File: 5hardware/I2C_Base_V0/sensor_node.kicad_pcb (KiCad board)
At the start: 2 copper layers, 99.5 x 99.5 mm, 264 parts, among them J2 PJ-320D-A, J3 Conn_02x06_Top_Bottom, J4 Conn_01x19_Socket, J5 Conn_01x19_Socket, J6 Conn_01x06_Socket, J7 Conn_01x04_Pin, J8 Conn_01x04_Pin, P1 S3B-PH-SM4-TB, P2 S4B-PH-SM4-TB, P3 S3B-PH-SM4-TB, Q2 Si2371EDS, Q3 Si2371EDS, SW2 SW_Push, SW3 SW_Push, U10 ESP-12F, U12 APDS-9960, U14 DS3231M, U3 CR2450, U4 CH32V003F4P6, U5 SHT31-DIS, U6 DS1307Z+, U7 XC6206PxxxMR, U8 TPL5110, U9 BH1750FVI-TR, Y1 Crystal, Y2 Crystal

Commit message: update PCB.
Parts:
- removed the C1 at (146.2, 141.2)
- removed the C1 at (96.2, 141.2)
- removed the C1 at (96.2, 91.2)
- removed the C1 at (146.2, 91.2)
- removed the C2 at (107.9, 75.8)
- removed the C2 at (57.9, 75.8)
- removed the C2 at (57.9, 125.8)
- removed the C2 at (107.9, 125.8)
- removed the C3 at (108.0, 64.8)
- removed the C3 at (58.0, 64.8)
- removed the C3 at (58.0, 114.8)
- removed the C3 at (108.0, 114.8)
- removed the C5 at (143.8, 125.5)
- removed the C5 at (93.8, 75.5)
- removed the C5 at (93.8, 125.5)
- removed the C5 at (143.8, 75.5)
- removed the C6 at (143.8, 70.8)
- removed the C6 at (93.8, 120.8)
- removed the C6 at (93.8, 70.8)
- removed the C6 at (143.8, 120.8)
- removed the D1 at (127.6, 77.2)
- removed the D1 at (127.6, 127.2)
- removed the D1 at (77.6, 77.2)
- removed the D1 at (77.6, 127.2)
- removed D10 (x4): LED, LED_SMD:LED_0603_1608Metric
- removed the D2 at (88.1, 113.8)
- removed the D2 at (138.1, 63.8)
- removed the D2 at (88.1, 63.8)
- removed the D2 at (138.1, 113.8)
- removed the D3 at (130.5, 124.0)
- removed the D3 at (80.5, 124.0)
- removed the D3 at (80.5, 74.0)
- removed the D3 at (130.5, 74.0)
- removed the D4 at (140.0, 120.5)
- removed the D4 at (90.0, 120.5)
- removed the D4 at (90.0, 70.5)
- removed the D4 at (140.0, 70.5)
- removed the D5 at (81.5, 90.5)
- removed the D5 at (131.5, 90.5)
- removed the D5 at (131.5, 140.5)
- removed the D5 at (81.5, 140.5)
- removed the D6 at (76.0, 108.8)
- removed the D6 at (126.0, 108.8)
- removed the D6 at (126.0, 58.8)
- removed the D6 at (76.0, 58.8)
- removed the J2 at (75.4, 87.7)
- removed the J2 at (125.4, 137.7)
- removed the J2 at (75.4, 137.7)
- removed the J2 at (125.4, 87.7)
- removed the J3 at (94.9, 53.6)
- removed the J3 at (144.9, 53.6)
- removed the J3 at (94.9, 103.6)
- removed the J3 at (144.9, 103.6)
- removed the J4 at (97.7, 99.8)
- removed the J4 at (97.7, 49.8)
- removed the J4 at (147.7, 99.8)
- removed the J4 at (147.7, 49.8)
- removed the J5 at (97.7, 46.0)
- removed the J5 at (147.7, 46.0)
- removed the J5 at (147.7, 96.0)
- removed the J5 at (97.7, 96.0)
- removed J6 (x4): Conn_01x06_Socket, Connector_PinHeader_2.00mm:PinHeader_1x06_P2.00mm_Vertical
- removed J7 (x4), J8 (x4): Conn_01x04_Pin, Connector_PinHeader_1.27mm:PinHeader_1x04_P1.27mm_Vertical
- removed the P1 at (58.3, 133.1)
- removed the P1 at (108.3, 83.1)
- removed the P1 at (108.3, 133.1)
- removed the P1 at (58.3, 83.1)
- removed the P2 at (58.4, 70.2)
- removed the P2 at (108.3, 70.2)
- removed the P2 at (108.3, 120.2)
- removed the P2 at (58.4, 120.2)
- removed the P3 at (108.4, 57.4)
- removed the P3 at (108.4, 107.3)
- removed the P3 at (58.4, 57.4)
- removed the P3 at (58.4, 107.3)
- removed the Q2 at (124.3, 82.8)
- removed the Q2 at (74.3, 132.8)
- removed the Q2 at (124.3, 132.8)
- removed the Q2 at (74.3, 82.8)
- removed the Q3 at (120.4, 78.1)
- removed the Q3 at (70.4, 128.1)
- removed the Q3 at (70.4, 78.1)
- removed the Q3 at (120.4, 128.1)
- removed the R1 at (142.7, 119.8)
- removed the R1 at (92.7, 119.8)
- removed the R1 at (92.7, 69.8)
- removed the R1 at (142.7, 69.8)
- removed the R10 at (133.2, 90.5)
- removed the R10 at (133.2, 140.5)
- removed the R10 at (83.2, 90.5)
- removed the R10 at (83.2, 140.5)
- removed the R11 at (70.0, 87.8)
- removed the R11 at (120.0, 137.8)
- removed the R11 at (120.0, 87.8)
- removed the R11 at (70.0, 137.8)
- removed the R14 at (120.5, 59.3)
- removed the R14 at (70.5, 59.3)
- removed the R14 at (70.5, 109.3)
- removed the R14 at (120.5, 109.3)
- removed the R15 at (130.5, 60.7)
- removed the R15 at (80.5, 60.7)
- removed the R15 at (80.5, 110.7)
- removed the R15 at (130.5, 110.7)
- removed the R16 at (96.8, 138.0)
- removed the R16 at (146.8, 88.0)
- removed the R16 at (96.8, 88.0)
- removed the R16 at (146.8, 138.0)
- removed the R17 at (144.5, 137.9)
- removed the R17 at (94.5, 87.9)
- removed the R17 at (144.5, 87.9)
- removed the R17 at (94.5, 137.9)
- removed the R18 at (91.9, 103.9)
- removed the R18 at (141.9, 53.9)
- removed the R18 at (91.9, 53.9)
- removed the R18 at (141.9, 103.9)
- removed the R19 at (139.9, 103.9)
- removed the R19 at (89.9, 53.9)
- removed the R19 at (139.9, 53.9)
- removed the R19 at (89.9, 103.9)
- removed the R2 at (113.3, 126.8)
- removed the R2 at (113.3, 76.8)
- removed the R2 at (63.3, 76.8)
- removed the R2 at (63.3, 126.8)
- removed the R20 at (72.8, 87.8)
- removed the R20 at (72.8, 137.8)
- removed the R20 at (122.8, 87.8)
- removed the R20 at (122.8, 137.8)
- removed the R21 at (141.0, 109.8)
- removed the R21 at (141.0, 59.8)
- removed the R21 at (91.0, 59.8)
- removed the R21 at (91.0, 109.8)
- removed the R22 at (91.9, 107.6)
- removed the R22 at (141.9, 107.6)
- removed the R22 at (141.9, 57.6)
- removed the R22 at (91.9, 57.6)
- removed the R23 at (89.9, 107.6)
- removed the R23 at (139.9, 107.6)
- removed the R23 at (89.9, 57.6)
- removed the R23 at (139.9, 57.6)
- removed the R24 at (113.0, 133.5)
- removed the R24 at (63.0, 133.5)
- removed the R24 at (113.0, 83.5)
- removed the R24 at (63.0, 83.5)
- removed the R25 at (108.0, 112.0)
- removed the R25 at (58.0, 62.0)
- removed the R25 at (58.0, 112.0)
- removed the R25 at (108.0, 62.0)
- removed the R26 at (57.1, 52.5)
- removed the R26 at (57.1, 102.5)
- removed the R26 at (107.1, 52.5)
- removed the R26 at (107.1, 102.5)
- removed the R27 at (113.7, 68.8)
- removed the R27 at (63.7, 118.8)
- removed the R27 at (63.7, 68.8)
- removed the R27 at (113.7, 118.8)
- removed the R28 at (134.3, 71.2)
- removed the R28 at (134.3, 121.2)
- removed the R28 at (84.3, 71.2)
- removed the R28 at (84.3, 121.2)
- removed the R3 at (57.9, 128.2)
- removed the R3 at (107.9, 128.2)
- removed the R3 at (57.9, 78.2)
- removed the R3 at (107.9, 78.2)
- removed the R4 at (65.0, 79.5)
- removed the R4 at (115.0, 129.5)
- removed the R4 at (65.0, 129.5)
- removed the R4 at (115.0, 79.5)
- removed the R5 at (61.9, 79.5)
- removed the R5 at (111.9, 79.5)
- removed the R5 at (111.9, 129.5)
- removed the R5 at (61.9, 129.5)
- removed the R6 at (123.9, 128.5)
- removed the R6 at (123.9, 78.5)
- removed the R6 at (73.9, 128.5)
- removed the R6 at (73.9, 78.5)
- removed the R7 at (84.8, 126.0)
- removed the R7 at (134.8, 76.0)
- removed the R7 at (84.8, 76.0)
- removed the R7 at (134.8, 126.0)
- removed the R8 at (130.6, 128.2)
- removed the R8 at (80.6, 128.2)
- removed the R8 at (130.6, 78.2)
- removed the R8 at (80.6, 78.2)
- removed the R9 at (80.1, 133.0)
- removed the R9 at (130.1, 133.0)
- removed the R9 at (80.1, 83.0)
- removed the R9 at (130.1, 83.0)
- removed the SW2 at (63.7, 63.2)
- removed the SW2 at (113.7, 113.2)
- removed the SW2 at (113.7, 63.2)
- removed the SW2 at (63.7, 113.2)
- removed the SW3 at (88.5, 80.2)
- removed the SW3 at (88.5, 130.2)
- removed the SW3 at (138.5, 130.2)
- removed the SW3 at (138.5, 80.2)
- removed the U10 at (48.9, 105.2)
- removed the U10 at (48.9, 55.2)
- removed the U10 at (98.9, 55.2)
- removed the U10 at (98.9, 105.2)
- removed the U11 at (83.5, 73.5)
- removed the U11 at (83.5, 123.5)
- removed the U11 at (133.5, 73.5)
- removed the U11 at (133.5, 123.5)
- removed U12 (x4): APDS-9960, Sensor:Avago_APDS-9960
- removed the U14 at (76.0, 107.9)
- removed the U14 at (126.0, 107.9)
- removed the U14 at (76.0, 57.9)
- removed the U14 at (126.0, 57.9)
- removed the U2 at (99.2, 92.3)
- removed the U2 at (99.2, 142.3)
- removed the U2 at (149.2, 92.3)
- removed the U2 at (149.2, 142.3)
- removed the U3 at (122.0, 141.5)
- removed the U3 at (72.0, 91.5)
- removed the U3 at (122.0, 91.5)
- removed the U3 at (72.0, 141.5)
- removed the U4 at (72.6, 67.5)
- removed the U4 at (122.6, 67.5)
- removed the U4 at (72.6, 117.5)
- removed the U4 at (122.6, 117.5)
- removed the U5 at (97.3, 79.0)
- removed the U5 at (147.3, 79.0)
- removed the U5 at (97.3, 129.0)
- removed the U5 at (147.3, 129.0)
- removed the U6 at (138.2, 63.8)
- removed the U6 at (88.2, 63.8)
- removed the U6 at (88.2, 113.8)
- removed the U6 at (138.2, 113.8)
- removed the U7 at (132.8, 81.8)
- removed the U7 at (82.8, 81.8)
- removed the U7 at (82.8, 131.8)
- removed the U7 at (132.8, 131.8)
- removed the U8 at (68.4, 133.3)
- removed the U8 at (118.4, 83.3)
- removed the U8 at (68.4, 83.3)
- removed the U8 at (118.4, 133.3)
- removed the U9 at (147.3, 133.8)
- removed the U9 at (147.3, 83.8)
- removed the U9 at (97.3, 133.8)
- removed the U9 at (97.3, 83.8)
- removed Y1 (x4): Crystal, Crystal:Crystal_SMD_3215-2Pin_3.2x1.5mm
- removed Y2 (x4): Crystal, Crystal:Crystal_Round_D1.5mm_Vertical
- added C1: C, Capacitor_SMD:C_0805_2012Metric, F.Cu at (176.2, 59.5)
- added C10: C, Capacitor_SMD:C_0805_2012Metric, F.Cu at (192.8, 138.6)
- added C11: C, Capacitor_SMD:C_0805_2012Metric, F.Cu at (176.0, 87.5)
- added C2: C, Capacitor_SMD:C_0805_2012Metric, F.Cu at (155.9, 55.7)
- added C3: C, Capacitor_SMD:C_0805_2012Metric, F.Cu at (196.8, 56.4)
- added C4: C, Capacitor_SMD:C_0805_2012Metric, F.Cu at (158.8, 122.8)
- added C5: C, Capacitor_SMD:C_0805_2012Metric, F.Cu at (151.4, 61.1)
- added C6: C, Capacitor_SMD:C_0805_2012Metric, F.Cu at (164.8, 71.0)
- added C7: C, Capacitor_SMD:C_0805_2012Metric, F.Cu at (164.8, 74.6)
- added C8: C, Capacitor_SMD:C_0805_2012Metric, F.Cu at (159.5, 79.2)
- added C9: C, Capacitor_SMD:C_0805_2012Metric, F.Cu at (155.6, 119.3)
- added D1: LED, LED_SMD:LED_0603_1608Metric, F.Cu at (167.1, 49.2)
- added D11: LED, LED_SMD:LED_0603_1608Metric, F.Cu at (167.3, 139.6)
- added D2: D_Schottky, Diode_SMD:D_SOD-323, F.Cu at (152.1, 54.1)
- added D3: LED, LED_SMD:LED_0603_1608Metric, F.Cu at (157.1, 91.7)
- added D4: LED, LED_SMD:LED_0603_1608Metric, F.Cu at (156.0, 115.8)
- added D5: LED, LED_SMD:LED_0603_1608Metric, F.Cu at (176.0, 74.7)
- added D6: LL-R3528RGBC-008-B, R3528RGB:LED_LL-R3528RGBC-008-B, F.Cu at (163.2, 130.4)
- added D7: LED, LED_SMD:LED_0603_1608Metric, F.Cu at (164.6, 139.6)
- added D8: LED, LED_SMD:LED_0603_1608Metric, F.Cu at (167.1, 52.7)
- added D9: LED, LED_SMD:LED_0603_1608Metric, F.Cu at (164.1, 55.5)
- added J1: Conn_01x39_Socket, Connector_PinSocket_2.54mm:PinSocket_1x39_P2.54mm_Vertical, F.Cu at (171.0, 43.6)
- added J2: PJ-320D-A, A_SensorNode:PJ-320D, F.Cu at (150.3, 101.1)
- added J3: USB_C_Receptacle_USB2.0, Connector_USB:USB_C_Receptacle_G-Switch_GT-USB-7010ASV, F.Cu at (149.3, 112.3)
- added J4: Conn_01x39_Socket, Connector_PinSocket_2.54mm:PinSocket_1x39_P2.54mm_Vertical, F.Cu at (201.2, 43.6)
- added J5: Conn_01x15_Pin, Connector_PinHeader_2.54mm:PinHeader_1x15_P2.54mm_Vertical, F.Cu at (146.9, 44.0)
- added P1: S3B-PH-SM4-TB, S3B-PH:JST_S3B-PH-SM4-TB, F.Cu at (184.2, 133.8)
- added P2: S4B-PH-SM4-TB, S4B-PH:JST_S4B-PH-SM4-TB, F.Cu at (153.1, 88.8)
- added P3: S3B-PH-SM4-TB, S3B-PH:JST_S3B-PH-SM4-TB, F.Cu at (159.3, 51.0)
- added Q1: Si2371EDS, Package_TO_SOT_SMD:SOT-23, F.Cu at (186.4, 97.6)
- added Q2: Si2371EDS, Package_TO_SOT_SMD:SOT-23, F.Cu at (158.7, 60.3)
- added Q3: Si2371EDS, Package_TO_SOT_SMD:SOT-23, F.Cu at (166.2, 105.5)
- added Q5: MMBT5551L, Package_TO_SOT_SMD:SOT-23, F.Cu at (181.6, 97.6)
- added R1: R, Resistor_SMD:R_0805_2012Metric, F.Cu at (180.5, 129.3)
- added R10: R, Resistor_SMD:R_0805_2012Metric, F.Cu at (181.5, 122.7)
- added R11: R, Resistor_SMD:R_0603_1608Metric, F.Cu at (162.0, 135.6)
- added R12: R, Resistor_SMD:R_0805_2012Metric, F.Cu at (164.5, 135.3)
- added R13: R, Resistor_SMD:R_0805_2012Metric, F.Cu at (167.1, 56.5)
- added R14: R, Resistor_SMD:R_0805_2012Metric, F.Cu at (167.3, 130.4)
- added R15: R, Resistor_SMD:R_0805_2012Metric, F.Cu at (166.2, 126.0)
- added R16: R, Resistor_SMD:R_0805_2012Metric, F.Cu at (196.8, 50.9)
- added R17: R, Resistor_SMD:R_0805_2012Metric, F.Cu at (196.8, 45.7)
- added R18: R, Resistor_SMD:R_0805_2012Metric, F.Cu at (181.0, 59.5)
- added R19: R, Resistor_SMD:R_0603_1608Metric, F.Cu at (163.8, 83.1)
- added R2: R, Resistor_SMD:R_0805_2012Metric, F.Cu at (161.0, 119.3)
- added R20: R, Resistor_SMD:R_0603_1608Metric, F.Cu at (151.2, 64.9)
- added R21: R, Resistor_SMD:R_0603_1608Metric, F.Cu at (151.9, 56.9)
- added R22: R, Resistor_SMD:R_0603_1608Metric, F.Cu at (166.1, 83.1)
- added R23: R, Resistor_SMD:R_0805_2012Metric, F.Cu at (166.5, 119.3)
- added R24: EVM3ESX50B12, EVM3ES:EMV3ESX50B12, F.Cu at (176.5, 68.2)
- added R25: R, Resistor_SMD:R_0805_2012Metric, F.Cu at (192.4, 59.8)
- added R26: R, Resistor_SMD:R_0805_2012Metric, F.Cu at (181.5, 125.8)
- added R27: R, Resistor_SMD:R_0603_1608Metric, F.Cu at (160.6, 83.1)
- added R28: R, Resistor_SMD:R_0603_1608Metric, F.Cu at (158.1, 83.1)
- added R29: R, Resistor_SMD:R_0603_1608Metric, F.Cu at (161.9, 139.6)
- added R3: R, Resistor_SMD:R_0805_2012Metric, F.Cu at (181.5, 119.5)
- added R30: R, Resistor_SMD:R_0805_2012Metric, F.Cu at (167.3, 135.3)
- added R31: R, Resistor_SMD:R_0603_1608Metric, F.Cu at (151.0, 48.9)
- added R32: R, Resistor_SMD:R_0603_1608Metric, F.Cu at (151.0, 50.9)
- added R33: R, Resistor_SMD:R_0603_1608Metric, F.Cu at (151.0, 44.8)
- added R34: R, Resistor_SMD:R_0603_1608Metric, F.Cu at (151.0, 46.8)
- added R35: R, Resistor_SMD:R_0805_2012Metric, F.Cu at (164.9, 122.8)
- added R36: R, Resistor_SMD:R_0603_1608Metric, F.Cu at (196.5, 79.6)
- added R37: R, Resistor_SMD:R_0603_1608Metric, F.Cu at (196.4, 85.3)
- added R38: R, Resistor_SMD:R_0805_2012Metric, F.Cu at (160.0, 55.6)
- added R39: R, Resistor_SMD:R_0805_2012Metric, F.Cu at (167.1, 45.5)
- added R4: R, Resistor_SMD:R_0603_1608Metric, F.Cu at (154.8, 60.1)
- added R40: R, Resistor_SMD:R_0805_2012Metric, F.Cu at (191.3, 97.1)
- added R41: R, Resistor_SMD:R_0805_2012Metric, F.Cu at (191.3, 100.0)
- added R42: R, Resistor_SMD:R_0805_2012Metric, F.Cu at (181.6, 101.8)
- added R43: R, Resistor_SMD:R_0805_2012Metric, F.Cu at (186.4, 101.8)
- added R44: R, Resistor_SMD:R_0805_2012Metric, F.Cu at (156.5, 94.7)
- added R45: R, Resistor_SMD:R_0805_2012Metric, F.Cu at (156.0, 111.9)
- added R46: R, Resistor_SMD:R_0805_2012Metric, F.Cu at (197.6, 75.4)
- added R47: R, Resistor_SMD:R_0805_2012Metric, F.Cu at (176.0, 83.2)
- added R48: R, Resistor_SMD:R_0805_2012Metric, F.Cu at (176.0, 78.8)
- added R5: R, Resistor_SMD:R_0603_1608Metric, F.Cu at (154.8, 64.1)
- added R6: R, Resistor_SMD:R_0603_1608Metric, F.Cu at (167.1, 101.5)
- added R7: R, Resistor_SMD:R_0805_2012Metric, F.Cu at (160.9, 126.0)
- added R8: R, Resistor_SMD:R_0805_2012Metric, F.Cu at (186.7, 129.3)
- added R9: R, Resistor_SMD:R_0603_1608Metric, F.Cu at (167.1, 60.5)
- added SW1: SW_Push, Button_Switch_SMD:SW_SPST_PTS810, F.Cu at (151.8, 69.4)
- added SW2: RotaryEncoder, A_SensorNode:RotaryEncoder_E11, F.Cu at (179.0, 93.8)
- added SW3: SW_Push, Button_Switch_SMD:SW_SPST_PTS810, F.Cu at (151.8, 77.4)
- added SW4: SW_Push, A_SensorNode:ButtonSwitch12mm_SMD, F.Cu at (180.3, 61.5)
- added U1: ~, A_SensorNode:JDY-Base, B.Cu at (157.9, 137.8)
- added U10: ESP-12F, A_SensorNode:ESP12_SMD, B.Cu at (197.2, 42.0)
- added U11: STM32L010F4Px, Package_SO:TSSOP-20_4.4x6.5mm_P0.65mm, B.Cu at (189.5, 81.0)
- added U14: Lolin_Base, A_SensorNode:LolinBase, F.Cu at (172.9, 90.1)
- added U15: APDS-9960, Sensor:Avago_APDS-9960, F.Cu at (159.5, 71.2)
- added U16: SHT31-DIS, Sensor_Humidity:Sensirion_DFN-8-1EP_2.5x2.5mm_P0.5mm_EP1.1x1.7mm, F.Cu at (164.5, 78.8)
- added U17: DS1307Z+, Package_SO:SOIC-8_3.9x4.9mm_P1.27mm, F.Cu at (189.7, 123.9)
- added U18: DS3231M, Package_SO:SOIC-16W_7.5x10.3mm_P1.27mm, F.Cu at (186.0, 110.9)
- added U19: BH1750FVI-TR, BH1750:XDCR_BH1750FVI-TR, F.Cu at (159.2, 75.4)
- added U2: ESP32-C3-WROOM-02, ESP32-C3:MODULE_ESP32-C3-WROOM-02-H4, F.Cu at (184.2, 47.3)
- added U3: CR2450, Battery:BatteryHolder_ComfortableElectronic_CH273-2450_1x2450, F.Cu at (146.8, 120.3)
- added U4: CH32V003F4P6, Package_SO:TSSOP-20_4.4x6.5mm_P0.65mm, F.Cu at (163.1, 112.5)
- added U5: ~, A_SensorNode:E104-BT07, B.Cu at (167.3, 43.3)
- added U6: MCP1700x-330xxTO, Package_TO_SOT_THT:TO-92_Inline, F.Cu at (163.9, 65.9)
- added U7: XC6206PxxxMR, Package_TO_SOT_SMD:SOT-23-3, F.Cu at (163.4, 60.1)
- added U8: TPL5110, Package_TO_SOT_SMD:SOT-23-6, F.Cu at (159.1, 65.1)
- added U9: E18-MS1-PCB, RF_Module:E18-MS1-PCB, B.Cu at (145.7, 102.3)
- added Y3: Crystal, Crystal:Crystal_Round_D1.5mm_Vertical, F.Cu at (193.4, 133.2)
- added Y4: Crystal, Crystal:Crystal_SMD_3215-2Pin_3.2x1.5mm, F.Cu at (192.5, 129.3)
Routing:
- net GND: track 846.6 -> 10.2 mm, vias 84 -> 0
- net VCC: track 1176.6 -> 473.6 mm, vias 40 -> 10
- net SCL (5): track 639.4 -> 0.00 mm, vias 16 -> 0
- net SDA (4): track 571.9 -> 0.00 mm, vias 12 -> 0
- net RX: track 393.2 -> 0.00 mm, vias 8 -> 0
- net TX: track 303.7 -> 0.00 mm, vias 4 -> 0
- net Bat-Vo: track 330.9 -> 40.6 mm, vias 4 -> 1
- net Bat-Vi: track 380.1 -> 106.5 mm, vias 12 -> 0
- net D3_RX: track 243.9 -> 0.00 mm, vias 8 -> 0
- net SDA0: track 0.00 -> 243.6 mm, vias 0 -> 8
- net RX1: track 0.00 -> 223.5 mm, vias 0 -> 8
- net SCL0: track 0.00 -> 217.3 mm, vias 0 -> 8
- net D1_TX: track 209.1 -> 0.00 mm, vias 4 -> 0
- net TX1: track 0.00 -> 177.9 mm, vias 0 -> 4
- net DONE: track 190.1 -> 13.7 mm, vias 12 -> 2
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- removed copper zone on B.Cu, net GND
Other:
- board size 99.5 x 99.5 mm -> 58 x 100 mm
- board text removed: "5V"
- board text removed: "ADDR"
- board text removed: "Bi"
- board text removed: "Bo"
- board text removed: "D15"
- board text removed: "DONE"
- board text removed: "DRV"
- board text removed: "DRX"
- board text removed: "DTX"
- board text removed: "ESP-Mess Baseboard V5.0"
- board text removed: "MOSI"
- board text removed: "PD2"
- board text removed: "RX"
- board text removed: "SCK"
- board text removed: "SCL"
- board text removed: "SDA"
- board text removed: "SVi"
- board text removed: "SVo"
- board text removed: "TX"
- board text removed: "The Future is here"
- board text removed: "V+"
- board text removed: "V-"
- board text removed: "V-CUT"
- board text removed: "Vi+"
- board text removed: "Vi-"
- board text removed: "Vin+"
- board text removed: "Vin-"
- board text removed: "Vo"

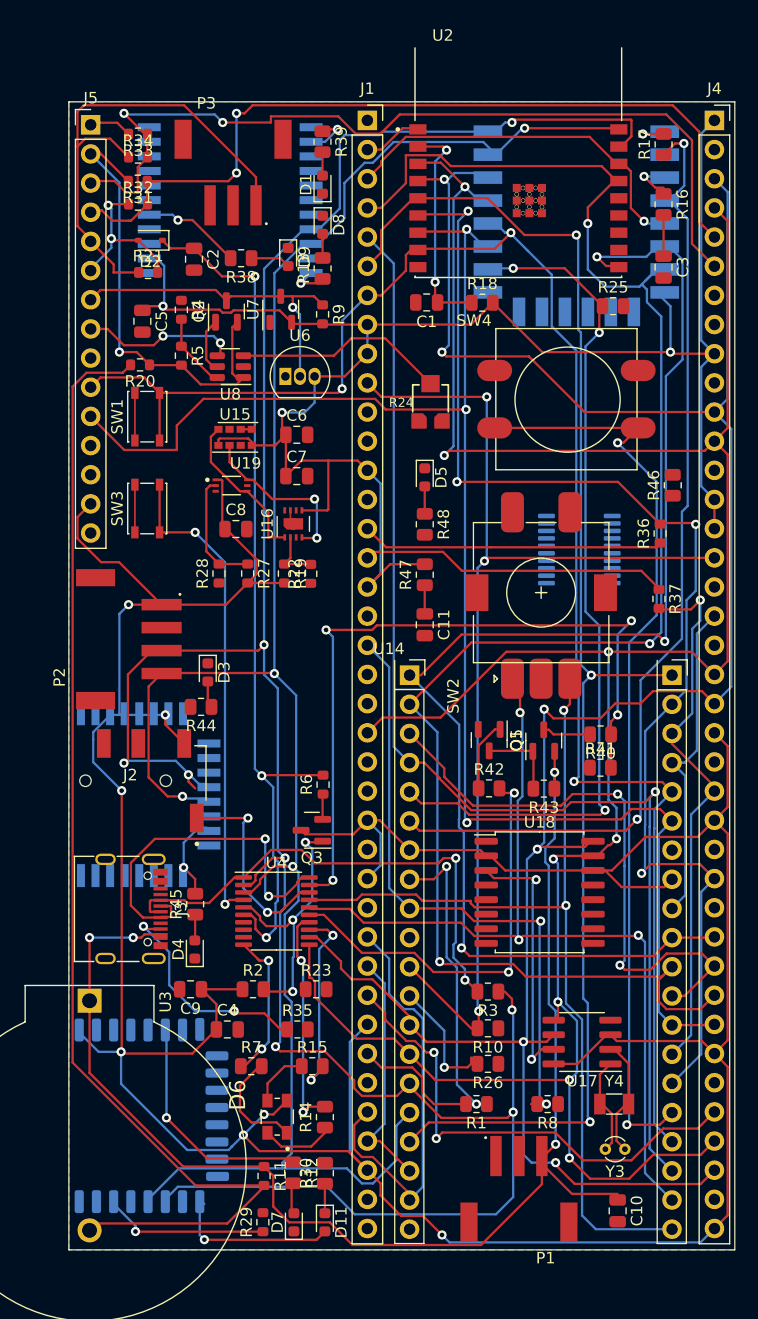
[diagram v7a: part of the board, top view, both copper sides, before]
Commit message: update schematic.
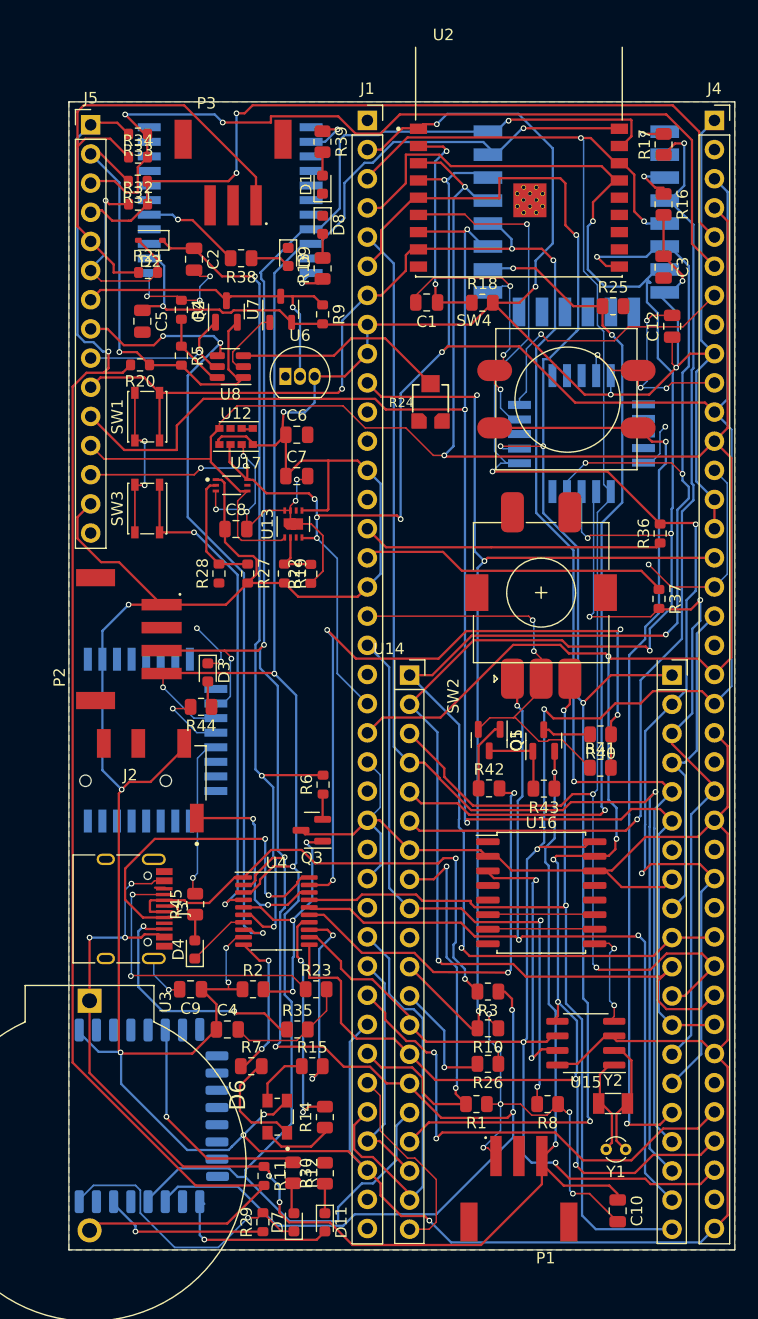
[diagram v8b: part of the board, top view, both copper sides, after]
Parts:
- removed C11: C, Capacitor_SMD:C_0805_2012Metric
- removed D5: LED, LED_SMD:LED_0603_1608Metric
- removed R46, R47, R48: R, Resistor_SMD:R_0805_2012Metric
- removed U11: STM32L010F4Px, Package_SO:TSSOP-20_4.4x6.5mm_P0.65mm
- removed U19: BH1750FVI-TR, BH1750:XDCR_BH1750FVI-TR
- removed Y3: Crystal, Crystal:Crystal_Round_D1.5mm_Vertical
- removed Y4: Crystal, Crystal:Crystal_SMD_3215-2Pin_3.2x1.5mm
- added C12: C, Capacitor_SMD:C_0805_2012Metric, F.Cu at (197.6, 61.5)
- added U12: APDS-9960, Sensor:Avago_APDS-9960, F.Cu at (159.6, 71.2)
- added U13: SHT31-DIS, Sensor_Humidity:Sensirion_DFN-8-1EP_2.5x2.5mm_P0.5mm_EP1.1x1.7mm, F.Cu at (164.6, 78.8)
- added Y1: Crystal, Crystal:Crystal_Round_D1.5mm_Vertical, F.Cu at (193.5, 133.2)
- added Y2: Crystal, Crystal:Crystal_SMD_3215-2Pin_3.2x1.5mm, F.Cu at (192.4, 129.2)
- J3: footprint Connector_USB:USB_C_Receptacle_G-Switch_GT-USB-7010ASV -> Connector_USB:USB_C_Receptacle_HRO_TYPE-C-31-M-12
- U15: value APDS-9960 -> DS1307Z+; footprint Sensor:Avago_APDS-9960 -> Package_SO:SOIC-8_3.9x4.9mm_P1.27mm
- U16: value SHT31-DIS -> DS3231M; footprint Sensor_Humidity:Sensirion_DFN-8-1EP_2.5x2.5mm_P0.5mm_EP1.1x1.7mm -> Package_SO:SOIC-16W_7.5x10.3mm_P1.27mm
- U17: value DS1307Z+ -> BH1750FVI-TR; footprint Package_SO:SOIC-8_3.9x4.9mm_P1.27mm -> BH1750:XDCR_BH1750FVI-TR
- U18: value DS3231M -> ~; footprint Package_SO:SOIC-16W_7.5x10.3mm_P1.27mm -> A_SensorNode:E220-900MM; moved to B.Cu
- moved U15 61.0 mm to (190.0, 124.0), turned to 180 degrees
- moved U17 57.3 mm to (159.2, 75.4), turned to 0 degrees
- moved U16 38.7 mm to (186.2, 110.9), turned to 0 degrees
- moved U18 34.4 mm to (193.2, 77.2), turned to 90 degrees
- moved U9 4.79 mm to (146.3, 97.6)
- moved U2 0.07 mm to (184.2, 47.2)
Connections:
- J4 pad 7: unconnected-(J4-Pin_7-Pad7) -> ANT0
- R19 pad 1: Net-(U16-ADDR) -> Net-(U13-ADDR)
- R22 pad 2: Net-(U16-ADDR) -> Net-(U13-ADDR)
- R27 pad 1: Net-(U19-ADDR) -> Net-(U17-ADDR)
- R28 pad 2: Net-(U19-ADDR) -> Net-(U17-ADDR)
- U15 pad 1: SDA0 -> Net-(U15-X1)
- U15 pad 2: unconnected-(U15-INT-Pad2) -> Net-(U15-X2)
- U15 pad 3: Net-(U15-LDR) -> VCC
- U15 pad 4: Net-(U15-LDR) -> GND
- U15 pad 5: VCC -> SDA0
- U15 pad 6: GND -> SCL0
- U15 pad 7: SCL0 -> Net-(U15-SQW/OUT)
- U16 pad 1: SDA0 -> unconnected-(U16-32KHZ-Pad1)
- U16 pad 2: Net-(U16-ADDR) -> VCC
- U16 pad 3: unconnected-(U16-ALERT-Pad3) -> Net-(U15-SQW/OUT)
- U16 pad 4: SCL0 -> unconnected-(U16-~{RST}-Pad4)
- U16 pad 5: VCC -> GND
- U16 pad 6: unconnected-(U16-~{RESET}-Pad6) -> GND
- U17 pad 1: Net-(U17-X1) -> VCC
- U17 pad 2: Net-(U17-X2) -> Net-(U17-ADDR)
- U17 pad 3: VCC -> GND
- U17 pad 4: GND -> SDA0
- U17 pad 5: SDA0 -> unconnected-(U17-DVI-Pad5)
- U18 pad 1: unconnected-(U18-32KHZ-Pad1) -> VCC
- U18 pad 10: GND -> DO2
- U18 pad 11: GND -> unconnected-(U18-BUSY-Pad11)
- U18 pad 12: GND -> MISO
- U18 pad 13: GND -> MOSI
- U18 pad 14: VCC -> DO3
- U18 pad 15: SDA0 -> SCK
- U18 pad 16: SCL0 -> GND
- U18 pad 2: VCC -> GND
- U18 pad 3: Net-(U17-SQW/OUT) -> unconnected-(U18-RST-Pad3)
- U18 pad 5: GND -> unconnected-(U18-NC-Pad5)
- U18 pad 6: GND -> ANT0
- U18 pad 8: GND -> unconnected-(U18-NC-Pad8)
- U18 pad 9: GND -> DO1
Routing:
- net GND: track 10.2 -> 313.5 mm, vias 0 -> 33
- net VCC: track 473.6 -> 533.4 mm, vias 10 -> 15
- net SCK: track 83.0 -> 141.4 mm, vias 3 -> 4
- net DONE: track 13.7 -> 71.4 mm, vias 2 -> 3
- net SCL0: track 217.3 -> 272.6 mm, vias 8 -> 12
- net SDA0: track 243.6 -> 281.6 mm
- net Net-(J3-CC1): track 0.00 -> 25.7 mm, vias 0 -> 2
- net Bat-Vi: track 106.5 -> 130.6 mm, vias 0 -> 1
- net ANT0: track 0.00 -> 23.9 mm, vias 0 -> 1
- net Net-(U17-SQW/OUT): track 22.8 -> 0.00 mm, vias 2 -> 0
- net Net-(U15-SQW/OUT): track 0.00 -> 22.8 mm, vias 0 -> 2
- net DO3: track 47.6 -> 65.1 mm, vias 1 -> 2
- net RX1: track 223.5 -> 206.1 mm, vias 8 -> 7
- net DO1: track 124.9 -> 138.9 mm, vias 3 -> 5
- net MOSI: track 153.0 -> 165.9 mm, vias 3 -> 5
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- added copper zone on B.Cu, net GND
